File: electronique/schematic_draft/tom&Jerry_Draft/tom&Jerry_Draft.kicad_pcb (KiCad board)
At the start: 4 copper layers, 54 x 57 mm, 188 parts, among them IC1001 NCS199A2RSQT2G, IC301 TCA9555RTWR, IC901 NCS199A2RSQT2G, J1201 Conn_01x02, J1301 Conn_01x02, J1401 Conn_01x02, J1501 Conn_01x02, J1601 Conn_02x05_Odd_FEMALE, J1602 Conn_02x05_Odd_FEMALE, J1603 Conn_02x05_Odd_FEMALE, J201 Conn_01x02, J202 USB_C_Receptacle_USB2.0_16P, J203 Conn_01x02, J204 Interrupteur, J301 FTSH-105-01-F-DV-P-TR, J302 FTSH-105-01-F-DV-P-TR, J303 FTSH-105-01-F-DV-P-TR, J304 FTSH-105-01-F-DV-P-TR, J305 Conn_01x08, J401 Conn_01x06, J402 Conn_01x06, J501 Conn_ST_STDC14, J601 Conn_01x03, J701 Conn_02x05_Odd_FEMALE, J702 Conn_02x05_Odd_FEMALE, J703 Conn_02x05_Odd_FEMALE, Q201 PMOS, SW501 SW_Push, SW502 SW_Push, SW503 SW_Push, U1001 ZXBM5210-S, U201 MP1475DJ-LF-P, U202 BQ25172DSGR, U301 ADXL343, U501 STM32G431CBU6, U601 PAM8302AAY, U801 LP5812ADSDR, U901 ZXBM5210-S, Y501 16MHz

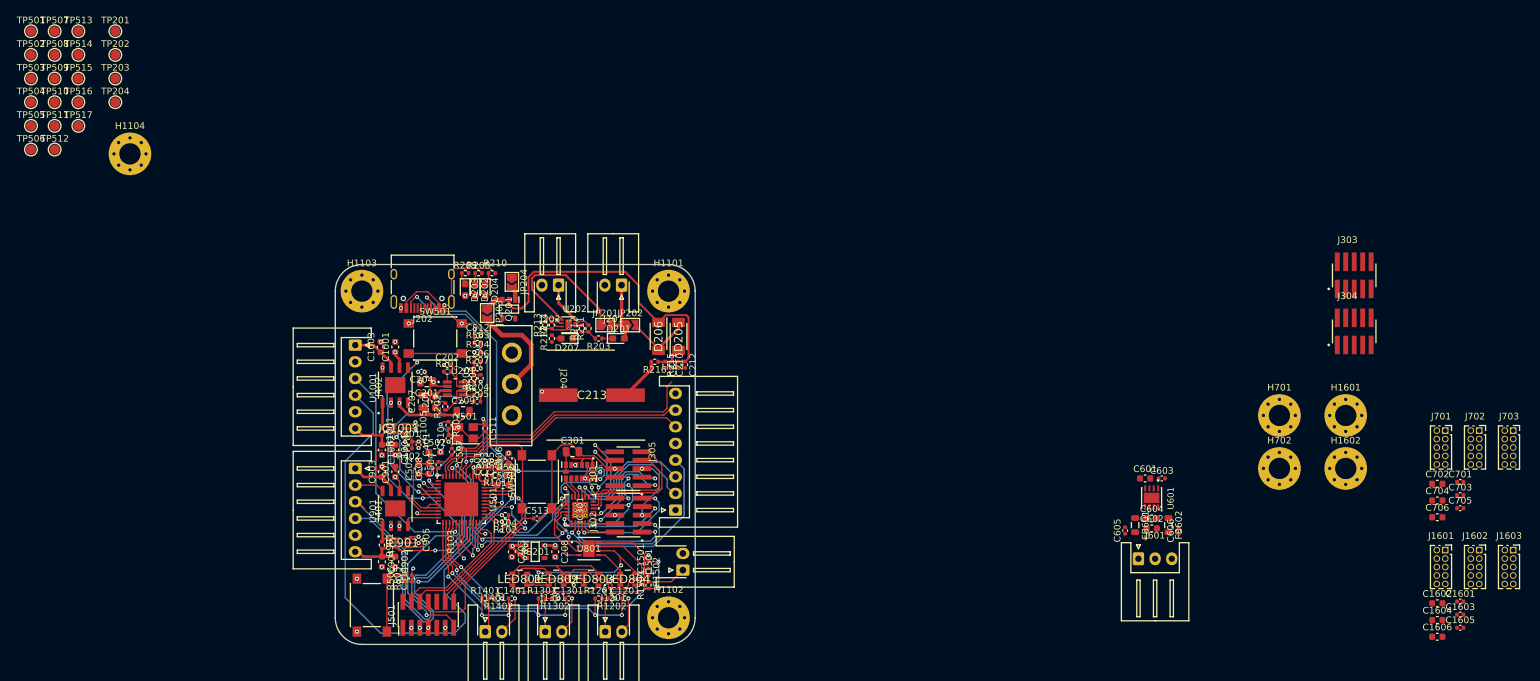
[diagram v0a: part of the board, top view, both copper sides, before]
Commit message: Routage Power
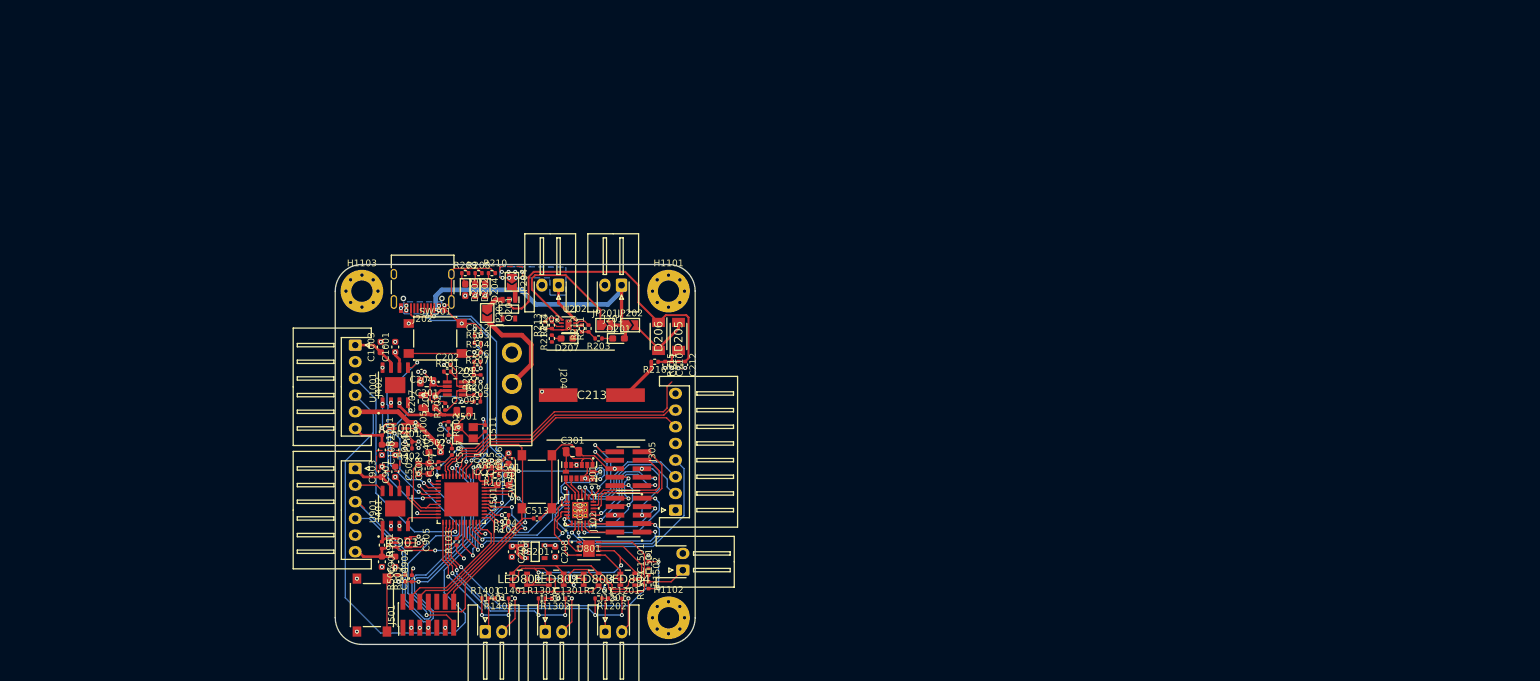
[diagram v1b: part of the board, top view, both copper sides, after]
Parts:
- removed C1601, C1603, C1605, C701, C703, C705: 100nF, Capacitor_SMD:C_0402_1005Metric
- removed C1602, C1604, C1606, C702, C704, C706: 4.7uF, Capacitor_SMD:C_0603_1608Metric
- removed C601, C604: 1u, Capacitor_SMD:C_0603_1608Metric
- removed C602: 10u, Capacitor_SMD:C_0603_1608Metric
- removed C603: 100n, Capacitor_SMD:C_0402_1005Metric
- removed C605, C606: 220p, Capacitor_SMD:C_0402_1005Metric
- removed FB601, FB602: FerriteBead_Small, Inductor_SMD:L_0805_2012Metric
- removed H1104, H1601, H1602, H701, H702: MountingHole_Pad, MountingHole:MountingHole_3.2mm_M3_Pad_Via
- removed J1601, J1602, J1603, J701, J702, J703: Conn_02x05_Odd_FEMALE, Connector_PinSocket_1.27mm:PinSocket_2x05_P1.27mm_Vertical
- removed J303, J304: FTSH-105-01-F-DV-P-TR, Tom&Jerry:SAMTEC_FTSH-105-01-F-DV-P-TR
- removed J601: Conn_01x03, Connector_JST:JST_XH_S3B-XH-A_1x03_P2.50mm_Horizontal
- removed TP201, TP202, TP203, TP204: TestPoint_Small, Test_Point:TestPoint_Pad_D1.5mm
- removed TP501: PC6, Test_Point:TestPoint_Pad_D1.5mm
- removed TP502: PB0, Test_Point:TestPoint_Pad_D1.5mm
- removed TP503: PB1, Test_Point:TestPoint_Pad_D1.5mm
- removed TP504: PB4, Test_Point:TestPoint_Pad_D1.5mm
- removed TP505: PB5, Test_Point:TestPoint_Pad_D1.5mm
- removed TP506: PB6, Test_Point:TestPoint_Pad_D1.5mm
- removed TP507: PB10, Test_Point:TestPoint_Pad_D1.5mm
- removed TP508: PB11, Test_Point:TestPoint_Pad_D1.5mm
- removed TP509: PA0, Test_Point:TestPoint_Pad_D1.5mm
- removed TP510: PA1, Test_Point:TestPoint_Pad_D1.5mm
- removed TP511: PA4, Test_Point:TestPoint_Pad_D1.5mm
- removed TP512: PA6, Test_Point:TestPoint_Pad_D1.5mm
- removed TP513: PA7, Test_Point:TestPoint_Pad_D1.5mm
- removed TP514: PA9, Test_Point:TestPoint_Pad_D1.5mm
- removed TP515: PA10, Test_Point:TestPoint_Pad_D1.5mm
- removed TP516: PA11, Test_Point:TestPoint_Pad_D1.5mm
- removed TP517: PA12, Test_Point:TestPoint_Pad_D1.5mm
- removed U601: PAM8302AAY, Tom&Jerry:DFN300X300X80-8N
- moved R103 0.30 mm to (92.2, 99.0)
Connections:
- U202 pad 10: GND -> (no net)
- U202 pad 11: GND -> (no net)
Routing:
- net /Alimentation/Batt_CHG: track 18.5 -> 43.8 mm, vias 0 -> 4
- net VCC: track 9.83 -> 28.6 mm
- net +3.3V: track 28.1 -> 45.4 mm, vias 15 -> 16
- net 1.65V: track 7.65 -> 23.2 mm
- net /Alimentation/CC1: track 58.6 -> 56.0 mm
- net /Alimentation/CC2: track 59.2 -> 58.0 mm
- net (no net): track 1.11 -> 0.00 mm
- net GND: track 101.1 -> 100.7 mm, vias 49 -> 52
- net Net-(IC1001-IN+): track 5.78 -> 5.85 mm, vias 0 -> 2
- net /Alimentation/Batt_cell: vias 0 -> 8
- added copper zone on In1.Cu, net +3.3V
- added copper zone on In1.Cu, net +5V
- added copper zone on B.Cu, net /Alimentation/Batt_CHG
- added copper zone on B.Cu, net /Alimentation/Batt_cell
- added copper zone on F.Cu, net /Alimentation/Batt_cell
- added copper zone on In2.Cu, net GND
- added copper zone on In1.Cu, net VCC

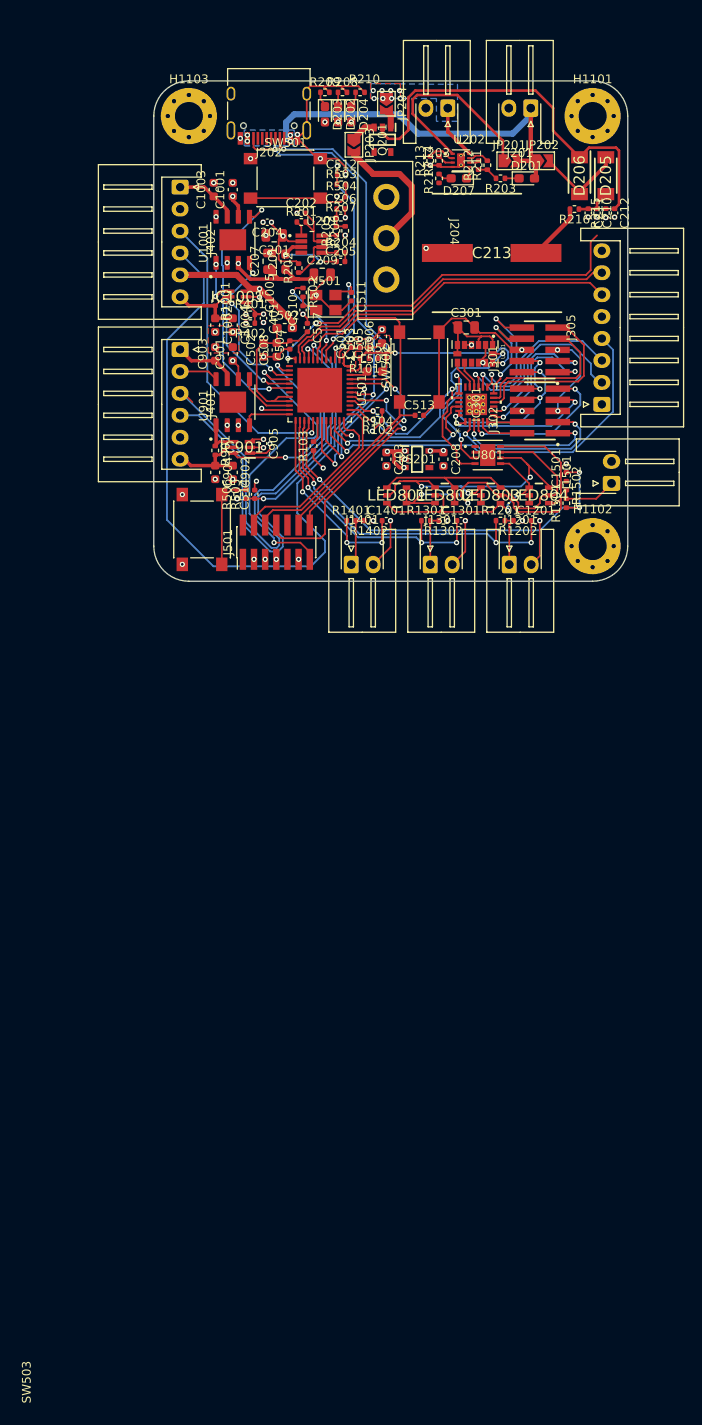
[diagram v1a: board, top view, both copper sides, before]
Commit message: V2.0 placement avec tout dessus
Aucun routage réalisé
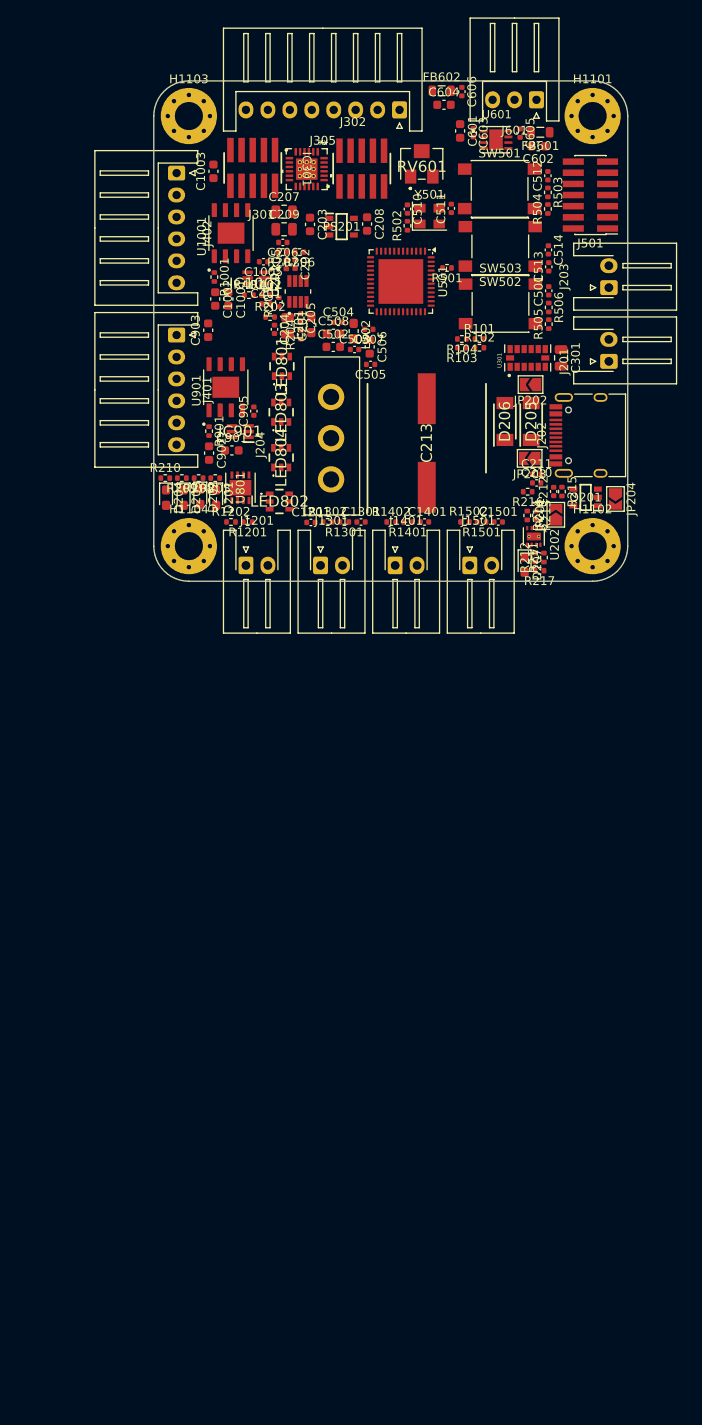
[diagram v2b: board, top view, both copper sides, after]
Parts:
- removed C1004, C904: 10uF, Capacitor_SMD:C_0603_1608Metric
- removed L501: 47n, Inductor_SMD:L_0603_1608Metric_Pad1.05x0.95mm_HandSolder
- added C601: 1u, Capacitor_SMD:C_0603_1608Metric, F.Cu at (108.9, 63.1)
- added C602: 10u, Capacitor_SMD:C_0603_1608Metric, F.Cu at (117.8, 64.8)
- added C603: 100n, Capacitor_SMD:C_0402_1005Metric, F.Cu at (110.4, 63.3)
- added C604: 1u, Capacitor_SMD:C_0603_1608Metric, F.Cu at (107.1, 60.1)
- added C605: 220p, Capacitor_SMD:C_0402_1005Metric, F.Cu at (115.7, 63.4)
- added C606: 220p, Capacitor_SMD:C_0402_1005Metric, F.Cu at (109.1, 58.6)
- added FB601: FerriteBead_Small, Inductor_SMD:L_0805_2012Metric, F.Cu at (118.0, 63.2)
- added FB602: FerriteBead_Small, Inductor_SMD:L_0805_2012Metric, F.Cu at (106.8, 58.5)
- added H1104: MountingHole_Pad, MountingHole:MountingHole_3.2mm_M3_Pad_Via, F.Cu at (78.0, 110.4)
- added J601: Conn_01x03, Connector_JST:JST_XH_S3B-XH-A_1x03_P2.50mm_Horizontal, F.Cu at (117.6, 59.5)
- added RV601: R_Potentiometer, Tom&Jerry:Potar, F.Cu at (104.5, 66.8)
- added U601: PAM8302AAY, Tom&Jerry:DFN300X300X80-8N, F.Cu at (113.0, 64.1)
- Y501: footprint Crystal:Crystal_SMD_3225-4Pin_3.2x2.5mm -> Crystal:Crystal_SMD_EuroQuartz_MT-4Pin_3.2x2.5mm
- moved J501 53.3 mm to (123.8, 70.4), turned to 180 degrees
- moved J202 52.8 mm to (123.8, 97.8), turned to 90 degrees
- moved JP204 52.0 mm to (126.6, 105.0)
- moved D201 50.8 mm to (81.1, 104.9), turned to -90 degrees
- moved R210 49.2 mm to (75.3, 102.7)
- moved D204 48.5 mm to (75.4, 104.9)
- moved R203 47.1 mm to (81.0, 102.7)
- moved R208 46.9 mm to (79.1, 102.7), turned to 180 degrees
- moved R209 46.9 mm to (77.2, 102.7), turned to 180 degrees
- moved Q201 46.9 mm to (123.2, 104.8), turned to 180 degrees
- moved D203 46.5 mm to (77.4, 104.9)
- moved D202 46.3 mm to (79.3, 104.8)
- moved R217 46.1 mm to (118.0, 113.2), turned to 180 degrees
- moved R211 45.2 mm to (118.5, 111.7)
- moved R212 45.2 mm to (117.5, 111.7)
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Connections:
- R501 pad 2: Net-(L501-Pad2) -> Net-(U501-PB8)
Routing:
- net GND: track 100.7 -> 0.00 mm, vias 52 -> 0
- net /Motors&Drivers/ENCODER_2B: track 78.9 -> 0.00 mm, vias 1 -> 0
- net /Alimentation/CC2: track 58.0 -> 0.00 mm, vias 3 -> 0
- net /Alimentation/CC1: track 56.0 -> 0.00 mm, vias 3 -> 0
- net /Motors&Drivers/ENCODER_1A: track 55.2 -> 0.00 mm, vias 1 -> 0
- net /Motors&Drivers/ENCODER_1B: track 53.8 -> 0.00 mm, vias 1 -> 0
- net /Périphériques/MOUSTACHE_4: track 47.5 -> 0.00 mm, vias 3 -> 0
- net /STM32/NRST: track 46.3 -> 0.00 mm
- net /Périphériques/LIDAR_M_CTR: track 46.0 -> 0.00 mm, vias 1 -> 0
- net Net-(D206-K): track 45.4 -> 0.00 mm
- net +3.3V: track 45.4 -> 0.00 mm, vias 16 -> 0
- net /Musique/DAC_STM+: track 44.3 -> 0.00 mm, vias 2 -> 0
- net /Alimentation/Batt_CHG: track 43.8 -> 0.00 mm, vias 4 -> 0
- net Net-(LED801-B-): track 43.3 -> 0.00 mm, vias 2 -> 0
- net /Périphériques/MOUSTACHE_1: track 40.6 -> 0.00 mm, vias 3 -> 0
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- removed copper zone on F.Cu, net +3.3V
- removed copper zone on In1.Cu, net +3.3V
- removed copper zone on In1.Cu, net +5V
- removed copper zone on B.Cu, net /Alimentation/Batt_CHG
- removed copper zone on B.Cu, net /Alimentation/Batt_cell
- removed copper zone on F.Cu, net /Alimentation/Batt_cell
- removed copper zone on F.Cu, net GND
- removed copper zone on In2.Cu, net GND
- removed copper zone on In1.Cu, net VCC

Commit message: Routage Signal Complet - PCB V2.0
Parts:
- removed the D201 at (81.1, 104.9)
- removed the D203 at (77.4, 104.9)
- removed the J301 at (85.3, 67.3)
- removed J302: FTSH-105-01-F-DV-P-TR, Tom&Jerry:SAMTEC_FTSH-105-01-F-DV-P-TR
- removed the R203 at (81.0, 102.7)
- removed the R209 at (77.2, 102.7)
- added C1601: 100nF, Capacitor_SMD:C_0402_1005Metric, F.Cu at (12.9, 26.8)
- added C1602: 4.7uF, Capacitor_SMD:C_0603_1608Metric, F.Cu at (9.46, 27.1)
- added C1603: 100nF, Capacitor_SMD:C_0402_1005Metric, F.Cu at (12.9, 28.8)
- added C1604: 4.7uF, Capacitor_SMD:C_0603_1608Metric, F.Cu at (9.46, 29.6)
- added C1605: 100nF, Capacitor_SMD:C_0402_1005Metric, F.Cu at (12.9, 30.8)
- added C1606: 4.7uF, Capacitor_SMD:C_0603_1608Metric, F.Cu at (9.46, 32.1)
- added C701: 100nF, Capacitor_SMD:C_0402_1005Metric, F.Cu at (12.9, 8.88)
- added C702: 4.7uF, Capacitor_SMD:C_0603_1608Metric, F.Cu at (9.46, 9.15)
- added C703: 100nF, Capacitor_SMD:C_0402_1005Metric, F.Cu at (12.9, 10.9)
- added C704: 4.7uF, Capacitor_SMD:C_0603_1608Metric, F.Cu at (9.46, 11.7)
- added C705: 100nF, Capacitor_SMD:C_0402_1005Metric, F.Cu at (12.9, 12.8)
- added C706: 4.7uF, Capacitor_SMD:C_0603_1608Metric, F.Cu at (9.46, 14.2)
- added D205: LED, LED_SMD:LED_0603_1608Metric_Pad1.05x0.95mm_HandSolder, F.Cu at (77.3, 104.9)
- added D206: LED, LED_SMD:LED_0603_1608Metric_Pad1.05x0.95mm_HandSolder, F.Cu at (81.2, 104.9)
- added H1601: MountingHole_Pad, MountingHole:MountingHole_3.2mm_M3_Pad_Via, F.Cu at (3.48, 21.4)
- added H1602: MountingHole_Pad, MountingHole:MountingHole_3.2mm_M3_Pad_Via, F.Cu at (3.48, 29.4)
- added H701: MountingHole_Pad, MountingHole:MountingHole_3.2mm_M3_Pad_Via, F.Cu at (3.48, 3.48)
- added H702: MountingHole_Pad, MountingHole:MountingHole_3.2mm_M3_Pad_Via, F.Cu at (3.48, 11.4)
- added J1001: FTSH-105-01-F-DV-P-TR, Tom&Jerry:SAMTEC_FTSH-105-01-F-DV-P-TR, F.Cu at (98.0, 67.2)
- added J1601: Conn_02x05_Odd_FEMALE, Connector_PinSocket_1.27mm:PinSocket_2x05_P1.27mm_Vertical, F.Cu at (10.6, 19.1)
- added J1602: Conn_02x05_Odd_FEMALE, Connector_PinSocket_1.27mm:PinSocket_2x05_P1.27mm_Vertical, F.Cu at (15.7, 19.1)
- added J1603: Conn_02x05_Odd_FEMALE, Connector_PinSocket_1.27mm:PinSocket_2x05_P1.27mm_Vertical, F.Cu at (20.8, 19.1)
- added J701: Conn_02x05_Odd_FEMALE, Connector_PinSocket_1.27mm:PinSocket_2x05_P1.27mm_Vertical, F.Cu at (10.6, 1.18)
- added J701: FTSH-105-01-F-DV-P-TR, Tom&Jerry:SAMTEC_FTSH-105-01-F-DV-P-TR, F.Cu at (85.2, 67.2)
- added J702: Conn_02x05_Odd_FEMALE, Connector_PinSocket_1.27mm:PinSocket_2x05_P1.27mm_Vertical, F.Cu at (15.7, 1.18)
- added J703: Conn_02x05_Odd_FEMALE, Connector_PinSocket_1.27mm:PinSocket_2x05_P1.27mm_Vertical, F.Cu at (20.8, 1.18)
- added R215: 3.3k, Resistor_SMD:R_0402_1005Metric, F.Cu at (77.2, 102.7)
- added R216: 3.3k, Resistor_SMD:R_0402_1005Metric, F.Cu at (81.0, 102.7)
- moved C213 12.2 mm to (86.3, 75.9), turned to 90 degrees
- moved C512 7.35 mm to (93.5, 84.5), turned to 90 degrees
- moved R205 6.94 mm to (93.2, 72.7), turned to -90 degrees
- moved PS201 6.75 mm to (89.4, 77.1)
- moved R207 4.56 mm to (92.1, 72.6), turned to -90 degrees
- moved R206 4.47 mm to (89.9, 72.6)
- moved C502 3.23 mm to (95.5, 84.5), turned to -90 degrees
- moved C210 2.75 mm to (91.0, 74.3), turned to -90 degrees
- moved C604 2.73 mm to (106.5, 61.8), turned to 0 degrees
- moved C209 2.56 mm to (88.1, 79.9)
- moved R208 2.18 mm to (118.4, 103.6), turned to 0 degrees
- moved C211 2.03 mm to (117.6, 104.6), turned to 180 degrees
- moved R502 1.73 mm to (108.1, 77.1), turned to -90 degrees
- moved C203 1.60 mm to (87.2, 72.3)
- moved C212 1.50 mm to (92.2, 75.2)
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- renumbered C1005 to C1101, C1001 to C1102, C1002 to C1103, C1003 to C1104, C1201 to C1301, C1301 to C1401, C1401 to C1501, C1501 to C1601, C204 to C202, C207 to C203, C209 to C204, C210 to C206, C211 to C207, C213 to C208, C202 to C209, C206 to C210, C212 to C211, C203 to C212, C208 to C213, C511 to C501, C507 to C502, C508 to C503, C510 to C504, C502 to C505, C504 to C506, C513 to C507, C512 to C508, C514 to C509, C501 to C510, C503 to C511, C505 to C512, C506 to C513, C602 to C601, C604 to C602, C605 to C603, C601 to C604, C603 to C605, C905 to C901, C901 to C902, C902 to C903, C903 to C904, D205 to D201, D206 to D202, D207 to D203, D202 to D204, D204 to D207, H1101 to H1201, H1102 to H1202, H1103 to H1203, H1104 to H1204, IC1001 to IC1101, J1201 to J1301, J1301 to J1401, J1401 to J1501, J1501 to J1601, J204 to J201, J201 to J203, J203 to J204, J305 to J301, JP202 to JP201, JP203 to JP202, JP204 to JP203, JP201 to JP204, L502 to L501, LED804 to LED803, LED803 to LED804, R1001 to R1101, R1202 to R1301, R1201 to R1302, R1302 to R1401, R1301 to R1402, R1402 to R1501, R1401 to R1502, R1502 to R1601, R1501 to R1602, R204 to R201, R216 to R202, R202 to R203, R201 to R204, R207 to R206, R206 to R207, R215 to R208, R217 to R209, R211 to R210, R212 to R211, R213 to R212, R214 to R213, R208 to R214, R210 to R217, R502 to R501, R501 to R502, R504 to R503, R506 to R504, R503 to R505, R505 to R506, SW502 to SW501, SW501 to SW502, U1001 to U1101
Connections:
- IC301 pad 1: /Périphériques/TOF5_XSHUT -> /Périphériques/TOF6_XSHUT
- IC301 pad 14: /Périphériques/LIDAR_DEV_EN -> /Périphériques/LIDAR_M_EN
- IC301 pad 15: /Périphériques/LIDAR_M_EN -> /Périphériques/LIDAR_DEV_EN
- IC301 pad 16: /Périphériques/IMU_INT2 -> /Périphériques/IMU_INT1
- IC301 pad 17: /Périphériques/IMU_INT1 -> /Périphériques/IMU_INT2
- IC301 pad 2: /Périphériques/TOF4_GPIO1 -> /Périphériques/TOF6_GPIO1
- IC301 pad 3: /Périphériques/TOF4_XSHUT -> /Périphériques/TOF5_GPIO1
- IC301 pad 4: /Périphériques/TOF5_GPIO1 -> /Périphériques/TOF5_XSHUT
- IC301 pad 5: /Périphériques/TOF6_XSHUT -> /Périphériques/TOF4_GPIO1
- IC301 pad 6: /Périphériques/TOF6_GPIO1 -> /Périphériques/TOF4_XSHUT
- U202 pad 10: (no net) -> GND
- U202 pad 11: (no net) -> GND
- U501 pad 17: /Motors&Drivers/PWM_MOT2_CH1 -> /Motors&Drivers/PWM_MOT2_CH2
- U501 pad 18: /Motors&Drivers/PWM_MOT2_CH2 -> /Motors&Drivers/PWM_MOT2_CH1
- U501 pad 2: /STM32/BUTTON_Initial_State -> /STM32/BUTTON_Start_Robot
- U501 pad 25: /Périphériques/MOUSTACHE_3 -> /Périphériques/MOUSTACHE_1
- U501 pad 27: /Périphériques/MOUSTACHE_1 -> /Périphériques/MOUSTACHE_3
- U501 pad 29: /Motors&Drivers/ENCODER_2A -> /Motors&Drivers/ENCODER_2B
- U501 pad 3: /STM32/BUTTON_Start_Robot -> /STM32/BUTTON_Initial_State
- U501 pad 43: /Motors&Drivers/ENCODER_2B -> /Motors&Drivers/ENCODER_2A
- U501 pad 8: /Motors&Drivers/ENCODER_1B -> /Motors&Drivers/ENCODER_1A
- U501 pad 9: /Motors&Drivers/ENCODER_1A -> /Motors&Drivers/ENCODER_1B
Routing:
- net /Led_Debug/Led_Debug_SCL: track 0.00 -> 148.2 mm, vias 0 -> 4
- net /Led_Debug/Led_Debug_SDA: track 0.00 -> 112.2 mm, vias 0 -> 4
- net /Périphériques/LIDAR_M_CTR: track 0.00 -> 63.9 mm, vias 0 -> 1
- net /Périphériques/IMU_INT1: track 0.00 -> 57.7 mm, vias 0 -> 2
- net /Périphériques/IMU_INT2: track 0.00 -> 56.7 mm, vias 0 -> 2
- net /Motors&Drivers/ENCODER_2B: track 0.00 -> 45.5 mm, vias 0 -> 1
- net /Motors&Drivers/ENCODER_1B: track 0.00 -> 43.9 mm, vias 0 -> 1
- net /Motors&Drivers/ENCODER_1A: track 0.00 -> 43.8 mm, vias 0 -> 1
- net /Alimentation/CC1: track 0.00 -> 41.7 mm, vias 0 -> 3
- net /Motors&Drivers/ENCODER_2A: track 0.00 -> 41.4 mm, vias 0 -> 1
- net /STM32/VCP_RX: track 0.00 -> 40.4 mm, vias 0 -> 2
- net /Périphériques/EXPANDER_EXTI: track 0.00 -> 39.3 mm, vias 0 -> 2
- net /Périphériques/MOUSTACHE_1: track 0.00 -> 36.6 mm
- net /Motors&Drivers/ASSERV_I1: track 0.00 -> 36.4 mm, vias 0 -> 2
- net /Alimentation/Batt_cell: track 0.00 -> 36.3 mm, vias 0 -> 1
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- added copper zone on F.Cu, net +3.3V
